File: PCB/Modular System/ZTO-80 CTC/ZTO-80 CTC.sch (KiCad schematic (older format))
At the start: 16 parts, among them J1 ZTO-80 Bus, J2 Conn_01x02, J3 Conn_01x08, SW1 SW_DIP_x06, U1 Z80CTC, U2 74HC688

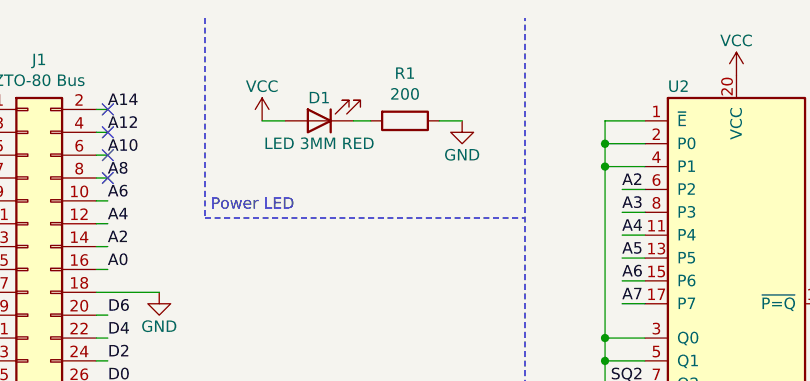
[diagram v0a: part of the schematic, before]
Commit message: Edited power LED resistor value
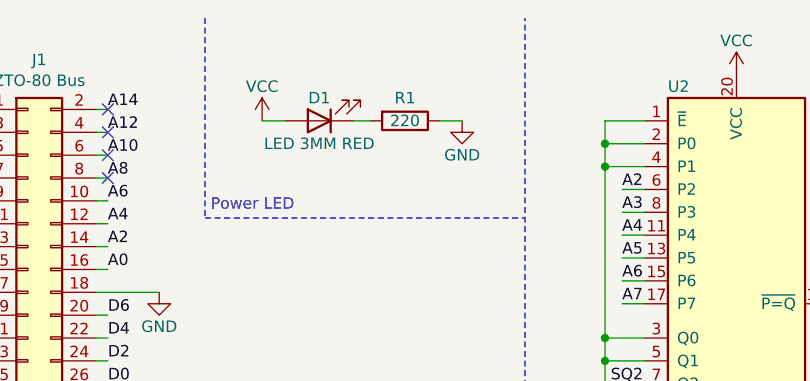
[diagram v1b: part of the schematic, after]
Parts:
- R1: value 200 -> 220
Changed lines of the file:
@@
 U 1 1 5E2B6523
 P 2825 925
-F 0 "R1" V 2618 925 50  0000 C CNN
-F 1 "200" V 2709 925 50  0000 C CNN
+F 0 "R1" V 2725 925 50  0000 C CNN
+F 1 "220" V 2825 925 50  0000 C CNN
 F 2 "Resistor_SMD:R_0805_2012Metric_Pad1.15x1.40mm_HandSolder" V 2755 925 50  0001 C CNN
 F 3 "~" H 2825 925 50  0001 C CNN

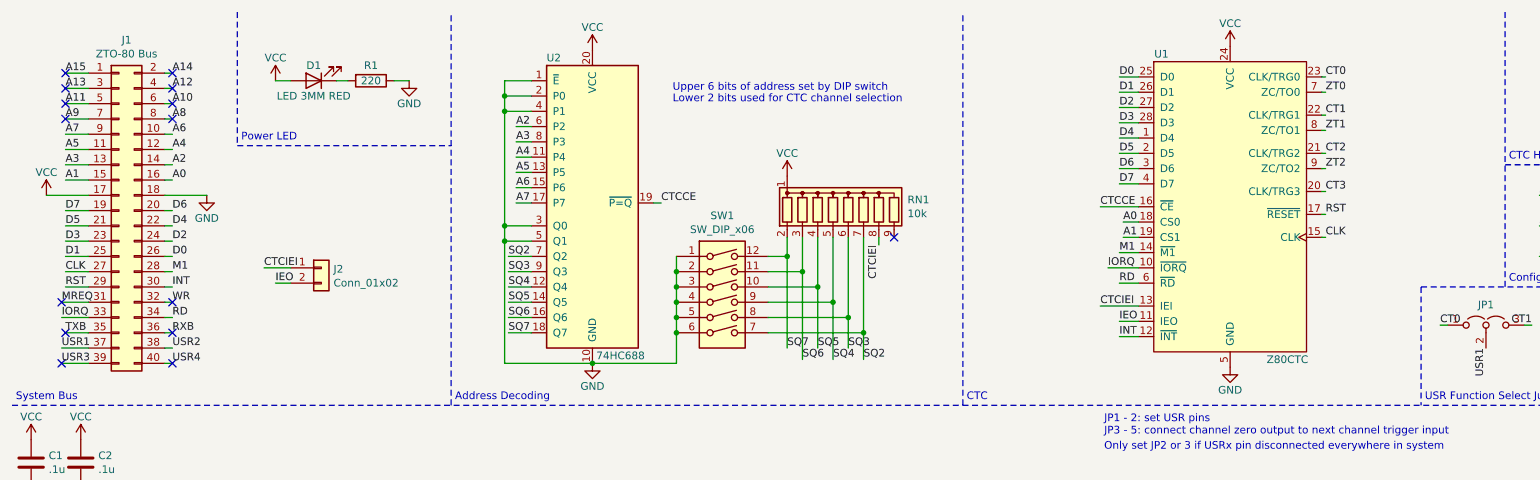
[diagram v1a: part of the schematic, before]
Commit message: Changed bus orientation
This change is backwards-compatible with all previous ZTO-80 modules
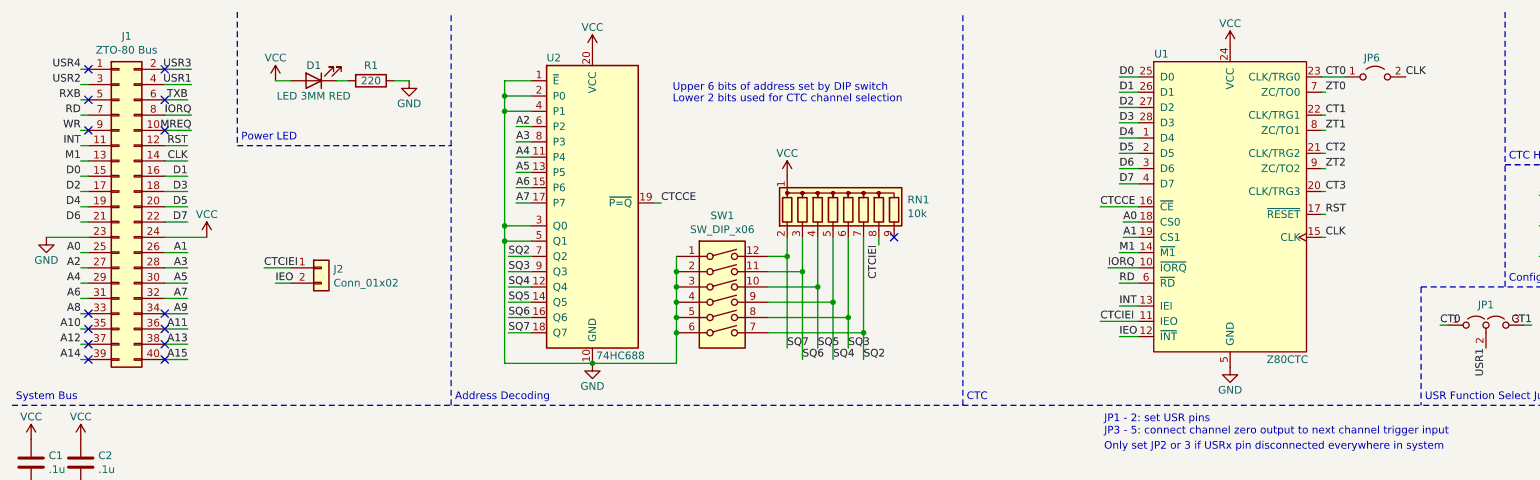
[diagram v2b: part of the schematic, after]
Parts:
- added JP6: Jumper_2_Open, Connector_PinHeader_2.54mm:PinHeader_1x02_P2.54mm_Vertical, symbol Jumper:Jumper_2_Open
- J1: footprint ZTO-80_Header:PinHeader_2x20_P2.54mm_Horizontal -> Connector_PinHeader_2.54mm:PinHeader_2x20_P2.54mm_Horizontal
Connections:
- net A0: now also J1.25 (Pin_25); no longer J1.16 (Pin_16)
- net A1: now also J1.26 (Pin_26); no longer J1.15 (Pin_15)
- net A10: now also J1.35 (Pin_35); no longer J1.6 (Pin_6)
- net A11: now also J1.36 (Pin_36); no longer J1.5 (Pin_5)
- net A12: now also J1.37 (Pin_37); no longer J1.4 (Pin_4)
- net A13: now also J1.38 (Pin_38); no longer J1.3 (Pin_3)
- net A14: now also J1.39 (Pin_39); no longer J1.2 (Pin_2)
- net A15: now also J1.40 (Pin_40); no longer J1.1 (Pin_1)
- net A2: now also J1.27 (Pin_27); no longer J1.14 (Pin_14)
- net A3: now also J1.28 (Pin_28); no longer J1.13 (Pin_13)
- net A4: now also J1.29 (Pin_29); no longer J1.12 (Pin_12)
- net A5: now also J1.30 (Pin_30); no longer J1.11 (Pin_11)
- net A6: now also J1.31 (Pin_31); no longer J1.10 (Pin_10)
- net A7: now also J1.32 (Pin_32); no longer J1.9 (Pin_9)
- net A8: now also J1.33 (Pin_33); no longer J1.8 (Pin_8)
- net A9: now also J1.34 (Pin_34); no longer J1.7 (Pin_7)
- net CLK: now also J1.14 (Pin_14), JP6.2 (B); no longer J1.27 (Pin_27)
- net CT0: now also JP6.1 (A)
- net CTCIEI: now also U1.11 (IEO); no longer U1.13 (IEI)
- net D0: now also J1.15 (Pin_15); no longer J1.26 (Pin_26)
- net D1: now also J1.16 (Pin_16); no longer J1.25 (Pin_25)
- net D2: now also J1.17 (Pin_17); no longer J1.24 (Pin_24)
- net D3: now also J1.18 (Pin_18); no longer J1.23 (Pin_23)
- net D4: now also J1.19 (Pin_19); no longer J1.22 (Pin_22)
- net D5: now also J1.20 (Pin_20); no longer J1.21 (Pin_21)
- net D6: now also J1.21 (Pin_21); no longer J1.20 (Pin_20)
- net D7: now also J1.22 (Pin_22); no longer J1.19 (Pin_19)
- net GND: now also J1.23 (Pin_23); no longer J1.18 (Pin_18)
- net IEO: now also U1.12 (~INT); no longer U1.11 (IEO)
- net INT: now also J1.11 (Pin_11), U1.13 (IEI); no longer J1.30 (Pin_30), U1.12 (~INT)
- net IORQ: now also J1.8 (Pin_8); no longer J1.33 (Pin_33)
- net M1: now also J1.13 (Pin_13); no longer J1.28 (Pin_28)
- net MREQ: now also J1.10 (Pin_10); no longer J1.31 (Pin_31)
- net RD: now also J1.7 (Pin_7); no longer J1.34 (Pin_34)
- net RST: now also J1.12 (Pin_12); no longer J1.29 (Pin_29)
- net RXB: now also J1.5 (Pin_5); no longer J1.36 (Pin_36)
- net TXB: now also J1.6 (Pin_6); no longer J1.35 (Pin_35)
- net USR1: now also J1.4 (Pin_4); no longer J1.37 (Pin_37)
- net USR2: now also J1.3 (Pin_3); no longer J1.38 (Pin_38)
- net USR3: now also J1.2 (Pin_2); no longer J1.39 (Pin_39)
- net USR4: now also J1.1 (Pin_1); no longer J1.40 (Pin_40)
- net VCC: now also J1.24 (Pin_24); no longer J1.17 (Pin_17)
- net WR: now also J1.9 (Pin_9); no longer J1.32 (Pin_32)

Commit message: Finished CTC
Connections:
- net ZT0: now also JP2.1 (A)
- net ZT1: now also JP2.3 (B); no longer JP2.1 (A)
- net ZT2: no longer JP2.3 (B)
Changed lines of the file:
@@
 $EndComp
 Text Label 10525 2525 0    50   ~ 0
+ZT0
+Text Label 11125 2525 2    50   ~ 0
 ZT1
-Text Label 11125 2525 2    50   ~ 0
-ZT2
 Wire Wire Line
 	11075 2525 11125 2525
